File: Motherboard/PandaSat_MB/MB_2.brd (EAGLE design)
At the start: 95.9 x 90.2 mm, 169 parts, among them J1 503182-1852, J2 10118194-0001LF, J3 DCJ0303, J7 BK-18650, Q13 IRLML2803, Q14 IRLML2803, Q15 IRLML2803, Q17 2N5088, Q2 32.768, U1 MAX706R, U11 DRV8848, U12 DRV8848, U2 LTC4121-4.2, U3 LSM9DS1, U4 PE014006, U5 MAX4372TEUK+T, U6 RFM23BP, U7 TPS54226PWPRPWP14_2P31X2P46-L, U8 ATSAMD51, U9 OKL-T3-W12, X1 BU-SMA-V

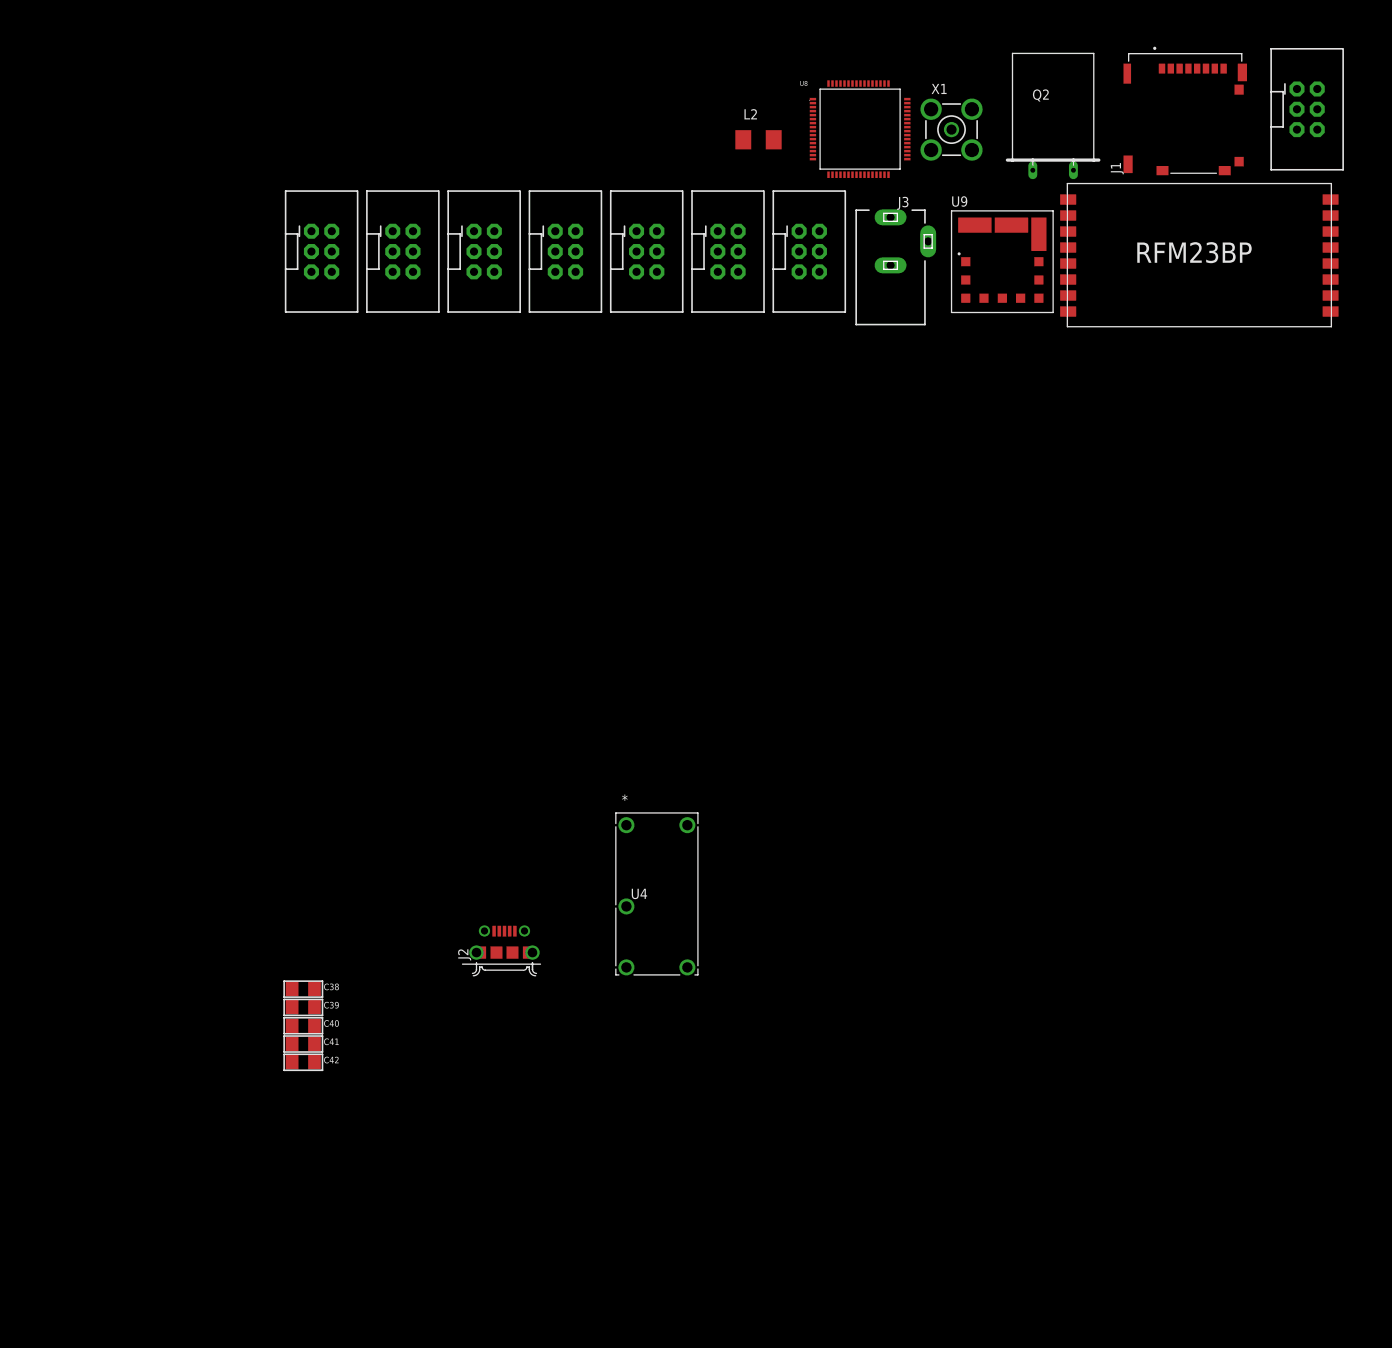
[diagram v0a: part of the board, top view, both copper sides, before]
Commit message: Changing connectors to SMD - not yet netted
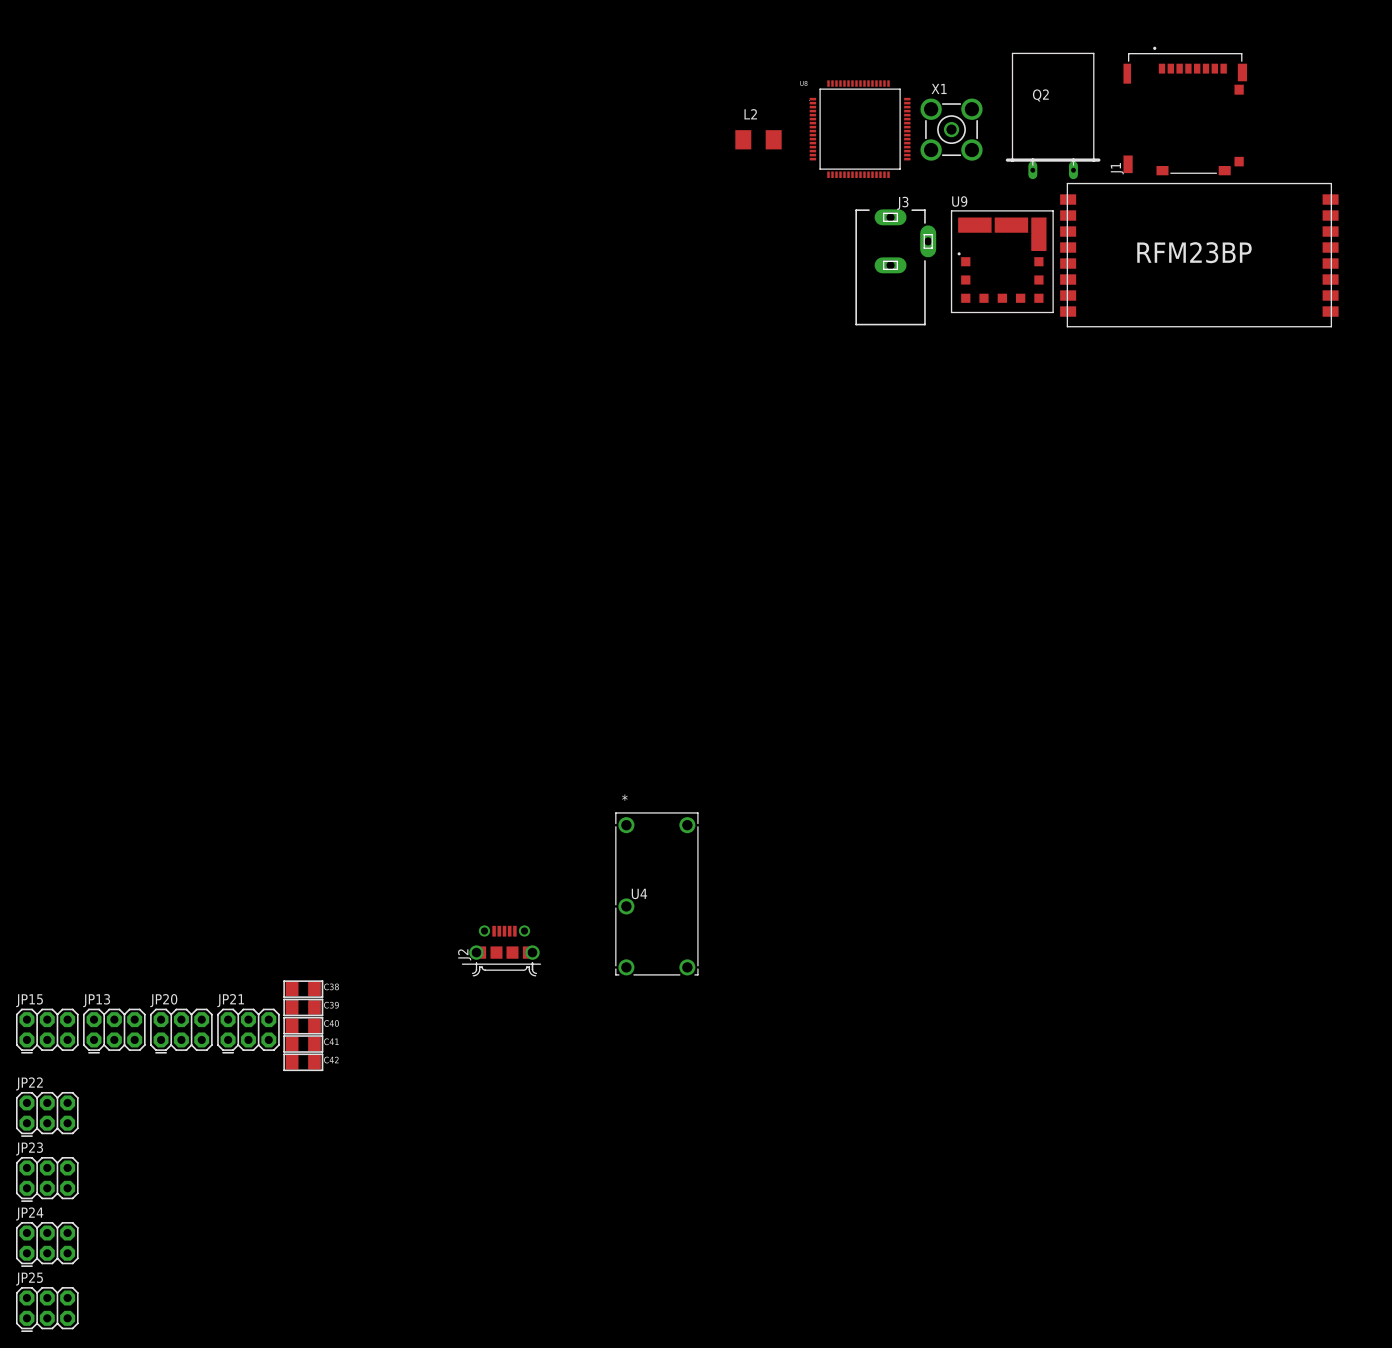
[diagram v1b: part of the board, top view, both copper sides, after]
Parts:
- removed JP14, JP16, JP17, JP19, JP6: (no value), SparkFun-Connectors:2X3-SHROUDED
- added JP21, JP22, JP23, JP24, JP25: (no value), SparkFun-Connectors:2X3
- JP13, JP15, JP20: device SparkFun-Connectors:2X3-SHROUDED -> SparkFun-Connectors:2X3
- moved JP20 184.5 mm to (-276.6, -20.8)
- moved JP13 126.5 mm to (-285.0, -20.8)
- moved JP15 119.3 mm to (-293.4, -20.8)
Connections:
- removed net MOY_MID: JP15.4, JP16.2
- removed net MOZ_MID: JP17.4, JP19.2
- removed net VBURN2: JP19.5, JP19.6
- new net N$63: JP13.3
- new net N$64: JP13.4
- new net N$65: JP13.2
- net !RESET: now also JP21.6; no longer JP20.6
- net 3.3V: now also JP21.1; no longer JP20.1, JP6.5
- net GND: now also JP20.1, JP21.5, JP24.1; no longer JP13.3, JP14.3, JP15.3, JP16.3, JP17.3, JP19.3, JP20.5, JP6.3
- net MOX_1: now also JP20.2; no longer JP13.2
- net MOX_2: now also JP24.3; no longer JP14.4
- net MOX_MID: now also JP20.3, JP24.2; no longer JP13.4, JP14.2
- net MOY_1: no longer JP15.2
- net MOY_2: no longer JP16.4
- net MOZ_1: no longer JP17.2
- net MOZ_2: no longer JP19.4
- net N$59: now also JP13.1; no longer JP13.5
- net PL_ENABLE: no longer JP6.2
- net PL_PWR_IN: no longer JP6.1
- net PL_UART_RX: no longer JP6.6
- net PL_UART_TX: no longer JP6.4
- net SWCLK: now also JP21.4; no longer JP20.4
- net SWDIO: now also JP21.2; no longer JP20.2
- net VBURN1: no longer JP17.5, JP17.6
- net VSOLAR: now also JP20.5, JP24.5; no longer JP13.1, JP14.1, JP15.1, JP16.1, JP17.1, JP19.1

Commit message: Finished with schematic, began placing components
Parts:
- moved JP21 282.1 mm to (-2.67, 74.3), turned to 90 degrees
- moved JP25 239.8 mm to (-89.7, 71.0), turned to 90 degrees
- moved Q1 236.4 mm to (-30.9, 13.3), flipped to the bottom, turned to 90 degrees
- moved U2 234.3 mm to (-59.8, 31.2), flipped to the bottom, turned to 180 degrees
- moved JP23 221.7 mm to (-90.0, 48.9), turned to 90 degrees
- moved JP24 221.5 mm to (-90.1, 40.4), turned to 90 degrees
- moved Q14 219.5 mm to (-70.2, 27.2), flipped to the bottom, turned to 180 degrees
- moved Q13 218.3 mm to (-70.3, 22.4), flipped to the bottom, turned to 180 degrees
- moved JP12 212.6 mm to (-43.0, 2.56)
- moved U$2 212.2 mm to (-83.4, 15.9), flipped to the bottom, turned to 270 degrees
- moved JP11 212.2 mm to (-34.6, 2.56)
- moved JP10 211.8 mm to (-26.4, 2.56)
- moved JP22 210.5 mm to (-90.1, 23.1), turned to 90 degrees
- moved JP13 210.3 mm to (-89.8, 57.4), turned to 90 degrees
- moved JP15 206.1 mm to (-90.3, 14.2), turned to 90 degrees
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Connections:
- removed net N$32: U$3.5, U$3.6, U$3.7, U$3.8
- removed net N$57: U$2.5, U$2.6, U$2.7, U$2.8
- removed net N$59: JP13.1
- removed net N$63: JP13.3
- removed net N$64: JP13.4
- removed net N$65: JP13.2
- new net MOY_MID: JP13.3, JP23.2
- new net MOZ_MID: JP15.3, JP22.2
- new net VBURN2: JP22.4, JP22.6, U$3.5, U$3.6, U$3.7, U$3.8
- net 3.3V: now also JP25.5
- net GND: now also JP13.1, JP15.1, JP22.1, JP23.1, JP25.3
- net MOY_1: now also JP13.2
- net MOY_2: now also JP23.3
- net MOZ_1: now also JP15.2
- net MOZ_2: now also JP22.3
- net PL_ENABLE: now also JP25.2
- net PL_PWR_IN: now also JP25.1
- net PL_UART_RX: now also JP25.6
- net PL_UART_TX: now also JP25.4
- net VBURN1: now also JP15.4, JP15.6, U$2.5, U$2.6, U$2.7, U$2.8
- net VSOLAR: now also JP13.5, JP15.5, JP22.5, JP23.5

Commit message: More component placing - power componente
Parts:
- moved R21 249.1 mm to (-38.5, 29.5), flipped to the bottom, turned to 180 degrees
- moved R40 240.3 mm to (-44.5, 15.9), flipped to the bottom
- moved R5 235.4 mm to (-52.9, 21.8), flipped to the bottom, turned to 180 degrees
- moved R1 232.5 mm to (-44.0, 29.5), flipped to the bottom, turned to 180 degrees
- moved C24 232.0 mm to (-44.5, 18.8), flipped to the bottom, turned to 180 degrees
- moved C20 218.6 mm to (-44.1, 26.4), flipped to the bottom, turned to 180 degrees
- moved R41 216.8 mm to (-48.1, 15.9), flipped to the bottom, turned to 180 degrees
- moved R37 215.9 mm to (-36.7, 68.1), flipped to the bottom, turned to 180 degrees
- moved C19 212.8 mm to (-48.6, 25.4), flipped to the bottom, turned to 90 degrees
- moved C9 210.1 mm to (-25.8, 20.5), flipped to the bottom
- moved C26 209.5 mm to (-67.3, 36.0), flipped to the bottom, turned to 90 degrees
- moved C22 208.6 mm to (-66.7, 24.0), flipped to the bottom, turned to 90 degrees
- moved C17 208.2 mm to (-47.0, 25.4), flipped to the bottom, turned to 90 degrees
- moved C25 207.8 mm to (-65.6, 36.1), flipped to the bottom, turned to 90 degrees
- moved C8 206.2 mm to (-25.8, 22.2), flipped to the bottom
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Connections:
- net GND: now also C39.2, C40.2, C41.2

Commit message: * Did Some initial Layout and found a few tasks to do [Listed in Commit Message] Trimmed a mm from long side of PCB Started Arranging Parts on Board
Todos:
Find Parts on Digikey/Mouser and add to BOM spreadsheet [in Documentation BOM]
Change Footprint on Crystal to SMD [Part in Documentation BOM]
Verify Footprints of Parts vs parts selected on BOM [package,  Pad Sizes, Pin 1 label]
Change Diode Symbols [3 on Battery Connections]
Change Foot Print of all 0603 parts to be same one [ Hand solder-able Dimensions] & also other size of passives
Change Reference designator for FETS from U$# -> Q#
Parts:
- removed FRAME1, FRAME2, FRAME3, FRAME4: FRAME-LETTER, SparkFun-Aesthetics:CREATIVE_COMMONS
- moved JP9 224.0 mm to (-38.6, 99.9)
- moved R15 223.7 mm to (-72.4, 36.3)
- moved Q15 221.1 mm to (-85.2, 17.7), turned to 270 degrees
- moved R13 217.3 mm to (-76.3, 36.4)
- moved R11 210.2 mm to (-81.5, 36.2), turned to 180 degrees
- moved JP8 206.1 mm to (-50.0, 100.0)
- moved R9 205.7 mm to (-74.6, 42.8)
- moved R10 204.0 mm to (-85.3, 36.3)
- moved R8 195.8 mm to (-83.4, 42.4), turned to 180 degrees
- moved LED2 175.9 mm to (-87.8, 101.1)
- moved LED1 169.1 mm to (-91.0, 101.2)
- moved D2 167.1 mm to (-84.4, 6.68), flipped to the bottom, turned to 90 degrees
- moved C14 160.9 mm to (-77.5, 58.1), turned to 270 degrees
- moved C13 159.6 mm to (-75.5, 58.0), turned to 270 degrees
- moved R18 155.3 mm to (-81.6, 27.1), turned to 270 degrees
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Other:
- board size 95.9 x 90.2 mm -> 93.9 x 89.2 mm

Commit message: Changed several components to fit BOM
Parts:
- removed D5: (no value), pandasat:SOD-128
- removed JP24: (no value), SparkFun-Connectors:2X3
- removed Q15: IRLML2803, maholli:SOT-23
- removed U12: DRV8848, pandasat:HTSSOP
- added D1: (no value), pandasat:SOD-128
- added J4: BU-SMA-V, con-coax:BU-SMA-V
- added J5: BK-18650, pandasat:BK-18650
- added K4: PE014006, maholli:RELAY5-PE_CO
- D2: value SBR2A40P1Q-7 -> (none); device BrownSpaceEngineering:PWRDI-123 -> pandasat:SOD-128
- D3: value (none) -> SBR2A40P1Q-7; device pandasat:SOD-128 -> BrownSpaceEngineering:PWRDI-123
- J7: value BK-18650 -> (none); device pandasat:BK-18650 -> SparkFun-Connectors:2X3
- Q1: value (none) -> IRLML2803; device transistor-power:SO-08 -> maholli:SOT-23
- Q2: value 32.768 -> IRLML2803; device special:Q -> maholli:SOT-23
- U10: value (none) -> DRV8848; device microbuilder:SOIC8_150MIL -> pandasat:HTSSOP
- U4: value PE014006 -> MAX4372TEUK+T; device maholli:RELAY5-PE_CO -> maholli:21-0057F
- U5: value MAX4372TEUK+T -> RFM23BP; device maholli:21-0057F -> RFM23BP:RFM23BP
- U6: value RFM23BP -> TPS54226PWPRPWP14_2P31X2P46-L; device RFM23BP:RFM23BP -> maholli:PWP14_2P31X2P46-L
- U7: value TPS54226PWPRPWP14_2P31X2P46-L -> ATSAMD51; device maholli:PWP14_2P31X2P46-L -> pandasat:TQFP64
- U8: value ATSAMD51 -> OKL-T3-W12; device pandasat:TQFP64 -> pandasat:OKL-T3-W12
- U9: value OKL-T3-W12 -> (none); device pandasat:OKL-T3-W12 -> microbuilder:SOIC8_150MIL
- X1: value BU-SMA-V -> (none); device con-coax:BU-SMA-V -> adafruit:NX3225
- moved Q1 183.7 mm to (-183.7, -21.8), turned to 0 degrees
- moved X1 170.0 mm to (-184.3, -25.2)
- moved U5 102.7 mm to (-26.6, 33.1)
- moved Q2 60.4 mm to (-85.2, 17.7)
- moved U4 56.5 mm to (-124.2, 1.01), turned to 0 degrees
- moved D2 53.2 mm to (-132.1, -17.0), flipped to the top
- moved D3 53.2 mm to (-84.4, 6.68), flipped to the bottom
- moved U6 46.3 mm to (-58.7, 66.4), turned to 270 degrees
- moved J7 43.2 mm to (-89.7, 61.5), flipped to the top, turned to 90 degrees
- moved U10 36.1 mm to (-82.3, 70.8), turned to 0 degrees
- moved U8 33.7 mm to (-23.1, 68.6), turned to 180 degrees
- moved U9 23.9 mm to (-46.7, 65.1), turned to 270 degrees
- moved U11 11.4 mm to (-82.2, 59.4)
- moved U7 9.53 mm to (-54.9, 57.7), turned to 0 degrees
- moved F2 4.30 mm to (-127.4, -21.6)
- renumbered JP13 to J8, JP15 to J10, JP20 to J6, JP21 to J12, JP22 to J11, JP23 to J9, JP25 to J13, L4 to L1, Q13 to Q3, Q14 to Q4, Q17 to Q8, U$1 to Q5, U$2 to Q6, U$3 to Q7
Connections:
- removed net N$40: D5.2, J3.1
- new net N$32: D1.2, J3.1
- net !RESET: now also U7.52; no longer U8.52
- net 3.3V: now also U4.3, U6.1, U7.21, U7.34, U7.48, U7.56, U7.8, U9.8; no longer U10.8, U5.3, U7.1, U8.21, U8.34, U8.48, U8.56, U8.8
- net 5V: now also U5.VCC, U8.4, U8.5; no longer U6.VCC, U9.4, U9.5
- net 5V2: now also D2.2; no longer D3.2
- net 5V_EN: now also Q1.1, U7.61; no longer Q1.4, U8.61
- net A5: now also U7.15; no longer U8.15
- net AIN: now also U7.16; no longer U8.16
- net AREF: now also U7.4; no longer U8.4
- net BURN_RELAY_A: now also U7.10; no longer U8.10
- net DXY_FAULT: now also U10.8, U7.59; no longer U11.8, U8.59
- net DZ_FAULT: now also U11.8, U7.60; no longer U12.8, U8.60
- net ENAB_BURN1: now also U7.27; no longer U8.27
- net ENAB_BURN2: now also U7.28; no longer U8.28
- net GND: now also J4.2, J4.3, J4.4, J4.5, J7.1, K4.12, Q2.2, U10.13, U10.3, U10.6, U10.PPAD, U4.1, U5.GND1, U5.GND2, U5.GND3, U6.15, U6.5, U6.8, U6.9, U7.22, U7.33, U7.47, U7.54, U7.7, U8.3, U9.4; no longer JP24.1, Q15.2, U10.4, U12.13, U12.3, U12.6, U12.PPAD, U4.12, U5.1, U6.GND1, U6.GND2, U6.GND3, U7.15, U7.5, U7.8, U7.9, U8.22, U8.33, U8.47, U8.54, U9.3, U9.7, X1.3, X1.5
- net I2C_SCL: now also U7.30; no longer U8.30
- net I2C_SDA: now also U7.29; no longer U8.29
- net I_BATT: now also U4.2, U7.14; no longer U5.2, U8.14
- net LED1: now also U7.64; no longer U8.64
- net LED2: now also U7.5; no longer U8.5
- net LED3: now also U7.31; no longer U8.31
- net LED4: now also U7.32; no longer U8.32
- net MINX_1: now also U10.16, U7.37; no longer U11.16, U8.37
- net MINX_2: now also U10.15, U7.38; no longer U11.15, U8.38
- net MINY_1: now also U10.9, U7.41; no longer U11.9, U8.41
- net MINY_2: now also U10.10, U7.42; no longer U11.10, U8.42
- net MINZ_1: now also U11.16, U7.43; no longer U12.16, U8.43
- net MINZ_2: now also U11.15, U7.44; no longer U12.15, U8.44
- net MOX_1: now also U10.2; no longer U11.2
- net MOX_2: now also J7.3, U10.4; no longer JP24.3, U11.4
- net MOX_MID: now also J7.2; no longer JP24.2
- net MOY_1: now also U10.7; no longer U11.7
- net MOY_2: now also U10.5; no longer U11.5
- net MOZ_1: now also U11.2; no longer U12.2
- net MOZ_2: now also U11.4; no longer U12.4
- net MXY_EN: now also U10.1, U7.6; no longer U11.1, U8.6
- net MZ_EN: now also U11.1, U7.9; no longer U12.1, U8.9
- net N$10: now also Q2.1; no longer Q15.1
- net N$12: now also Q2.3; no longer Q15.3
- net N$14: now also U6.12; no longer U7.12
- net N$18: now also U8.1; no longer Q1.1, Q1.3, U9.1
- net N$19: now also U8.6; no longer U9.6
- net N$22: now also U4.5; no longer U5.5
- net N$29: now also U7.1, X1.3; no longer Q2.2, U8.1
- net N$3: now also U6.10, U6.11; no longer U7.10, U7.11
- net N$30: now also J5.1, J5.2; no longer J7.1, J7.2
- net N$35: now also D3.A, K4.5; no longer D2.A, U4.5
- net N$36: now also J4.1, U5.ANT; no longer U6.ANT, X1.1
- net N$37: now also U5.GPIO_0, U5.RXON; no longer U6.GPIO_0, U6.RXON
- net N$39: now also U5.GPIO_1, U5.TXON; no longer U6.GPIO_1, U6.TXON
- net N$41: now also J5.3, J5.4, J5.7, J5.8; no longer J7.3, J7.4, J7.7, J7.8
- net N$42: now also U7.55; no longer U8.55
- net N$43: now also U7.53; no longer U8.53
- net N$44: now also U7.2, X1.1; no longer Q2.1, U8.2
- net N$46: now also U6.3; no longer U7.3
- net N$51: now also U6.4; no longer U7.4
- net N$52: now also U6.2; no longer U7.2
- net N$56: now also U7.3; no longer U8.3
- net PGOOD: now also U6.6; no longer U7.6
- net PL_ENABLE: now also U7.63; no longer U8.63
- net PL_PWR_EN: now also U7.62; no longer U8.62
- net PL_UART_RX: now also U7.40; no longer U8.40
- net PL_UART_TX: now also U7.39; no longer U8.39
- net P_GOOD: now also U7.51, U8.10; no longer U8.51, U9.10
- net QSPI_CS: now also U7.24, U9.1; no longer U10.1, U8.24
- net QSPI_DATA[0]: now also U7.17, U9.5; no longer U10.5, U8.17
- net QSPI_DATA[1]: now also U7.18, U9.2; no longer U10.2, U8.18
- net QSPI_DATA[2]: now also U7.19, U9.3; no longer U10.3, U8.19
- net QSPI_DATA[3]: now also U7.20, U9.7; no longer U10.7, U8.20
- net QSPI_SCK: now also U7.23, U9.6; no longer U10.6, U8.23
- net RF_NIRQ: now also U5.NIRQ, U7.12; no longer U6.NIRQ, U8.12
- net RF_SDN: now also U5.SDN, U7.11; no longer U6.SDN, U8.11
- net SPI_CS_RFM: now also U5.NSEL, U7.25; no longer U6.NSEL, U8.25
- net SPI_CS_SD: now also U7.26; no longer U8.26
- net SPI_MISO: now also U5.SDO, U7.49; no longer U6.SDO, U8.49
- net SPI_MOSI: now also U5.SDI, U7.50; no longer U6.SDI, U8.50
- net SPI_SCK: now also U5.SCK, U7.36; no longer U6.SCK, U8.36
- net SWCLK: now also U7.57; no longer U8.57
- net SWDIO: now also U7.58; no longer U8.58
- net USB_N: now also U7.45; no longer U8.45
- net USB_P: now also U7.46; no longer U8.46
- net VBATT: now also D3.C, K4.1, K4.14, Q1.3, U10.12, U4.4, U6.7; no longer D2.C, Q1.5, Q1.6, Q1.7, Q1.8, U12.12, U4.1, U4.14, U5.4, U7.7
- net VBATT_IN: now also D1.1, D2.1, J5.5, J5.6; no longer D3.1, D5.1, J7.5, J7.6
- net VBURN_A_IN: now also K4.11; no longer U4.11
- net VINT_1: now also U10.11, U10.14; no longer U11.11, U11.14
- net VINT_2: now also U11.11, U11.14; no longer U12.11, U12.14
- net VREG_IN: now also U6.13, U6.14, U8.2; no longer U7.13, U7.14, U9.2
- net VSOLAR: now also J7.5; no longer JP24.5
- net WDT_WDI: now also U7.35; no longer U8.35
